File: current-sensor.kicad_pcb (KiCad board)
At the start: 2 copper layers, 78 x 39.3 mm, 36 parts, among them J1 ‎0197134001‎, J2 ‎0197134001‎, J3 0731000105, J4 Molex_SL_01x02_Male, J5 Molex_SL_01x02_Male, SW1 PN12SHNA03QE, SW2 OS103011MA7QP1, SW3 OS103011MA7QP1, U1 ACS730xLCTR-20AB, U2 AD8616xRM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

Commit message: revision 1 of current sensor
- fix gain/bandwidth switch pin numbering
- move faston connectors further apart
- switch from MSOP to SOIC package for op-amp
- add silk labels to switches and connectors
- reduce LED resistor to increase brightness
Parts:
- R8: value 3.3k -> 2.2k
- U2, U3: footprint Package_SO:MSOP-8_3x3mm_P0.65mm -> Package_SO:SOIC-8_3.9x4.9mm_P1.27mm
- moved R6 2.00 mm to (142.0, 98.0)
- moved J2 1.50 mm to (153.5, 73.0)
- moved C6 0.75 mm to (138.5, 96.5)
- moved C7 0.75 mm to (150.5, 89.2)
- moved R5 0.75 mm to (138.5, 93.2)
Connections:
- SW2 pad 1: Net-(R1-Pad2) -> Net-(R2-Pad2)
- SW2 pad 2: Net-(R2-Pad2) -> Net-(R1-Pad2)
- SW3 pad 1: Net-(R5-Pad1) -> Net-(C3-Pad2)
- SW3 pad 2: Net-(C3-Pad2) -> Net-(R5-Pad1)
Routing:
- net /virtual_gnd: track 58.2 -> 36.4 mm
- net Net-(R5-Pad1): track 15.9 -> 31.0 mm
- net Net-(R1-Pad2): track 19.7 -> 33.0 mm
- net Net-(R2-Pad2): track 3.21 -> 5.33 mm
- net Net-(C3-Pad2): track 3.21 -> 5.33 mm
- net +5V: track 98.6 -> 97.5 mm
- net Net-(C5-Pad1): track 7.78 -> 6.84 mm
- net Net-(R7-Pad2): track 6.20 -> 7.09 mm
- net /current-: track 11.5 -> 12.1 mm, vias 30 -> 29
- net Net-(R2-Pad1): track 14.5 -> 15.1 mm
- net (no net): vias 1 -> 2
- added copper zone on F.Cu, net /virtual_gnd
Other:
- board text added: "Current Sensor r1 G. Keeth github.com/gkeeth/current-sensor 2020-12-07"
- board text removed: "Current Sensor r1 G. Keeth github.com/gkeeth/current-sensor 2020-11-10"

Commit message: add zero-current offset trim
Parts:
- added C10: 100n, Capacitor_SMD:C_0603_1608Metric, F.Cu at (155.2, 86.4)
- added R10: 1M, Resistor_SMD:R_0603_1608Metric, F.Cu at (162.5, 86.2)
- added R9: 33k, Resistor_SMD:R_0603_1608Metric, F.Cu at (160.0, 85.5)
- added RV1: 100k, Potentiometer_SMD:Potentiometer_Vishay_TS53YL_Vertical, F.Cu at (170.5, 86.8)
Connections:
- U3 pad 5: Net-(C5-Pad1) -> Net-(C10-Pad1)
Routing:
- net Net-(R10-Pad2): track 0.00 -> 10.0 mm
- net Net-(C10-Pad1): track 0.00 -> 7.95 mm
- net +5V: track 97.5 -> 104.6 mm
- net Net-(C5-Pad1): track 6.84 -> 3.79 mm
- net GND: track 14.6 -> 17.2 mm, vias 9 -> 11
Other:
- board text added: "Current Sensor r2 G. Keeth github.com/gkeeth/current-sensor 2021-01-03"
- board text added: "Zero Current Offset Trim Procedure: 1. set 1x gain 2. apply zero current (open circuit at current terminals) 3. adjust trimmer until zero-current voltage (BNC output) and BNC ground are the same 4. increase gain to 10x/100x and fine-tune adjustment"
- board text removed: "Current Sensor r1 G. Keeth github.com/gkeeth/current-sensor 2020-12-07"

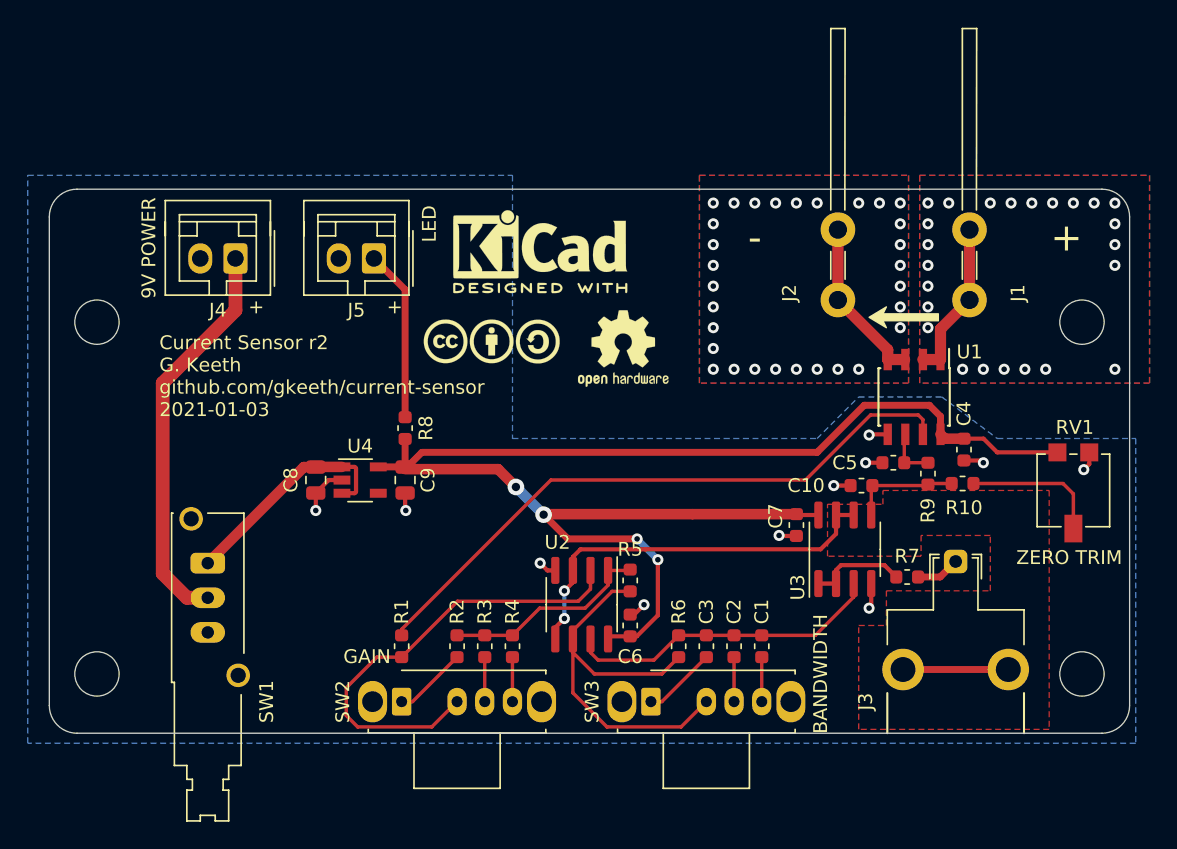
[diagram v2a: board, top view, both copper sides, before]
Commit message: Change offset trim circuit
completely ignore reference output from current sensor IC. Instead, use
trimpot to get 2.5V +/- 200mV reference voltage.
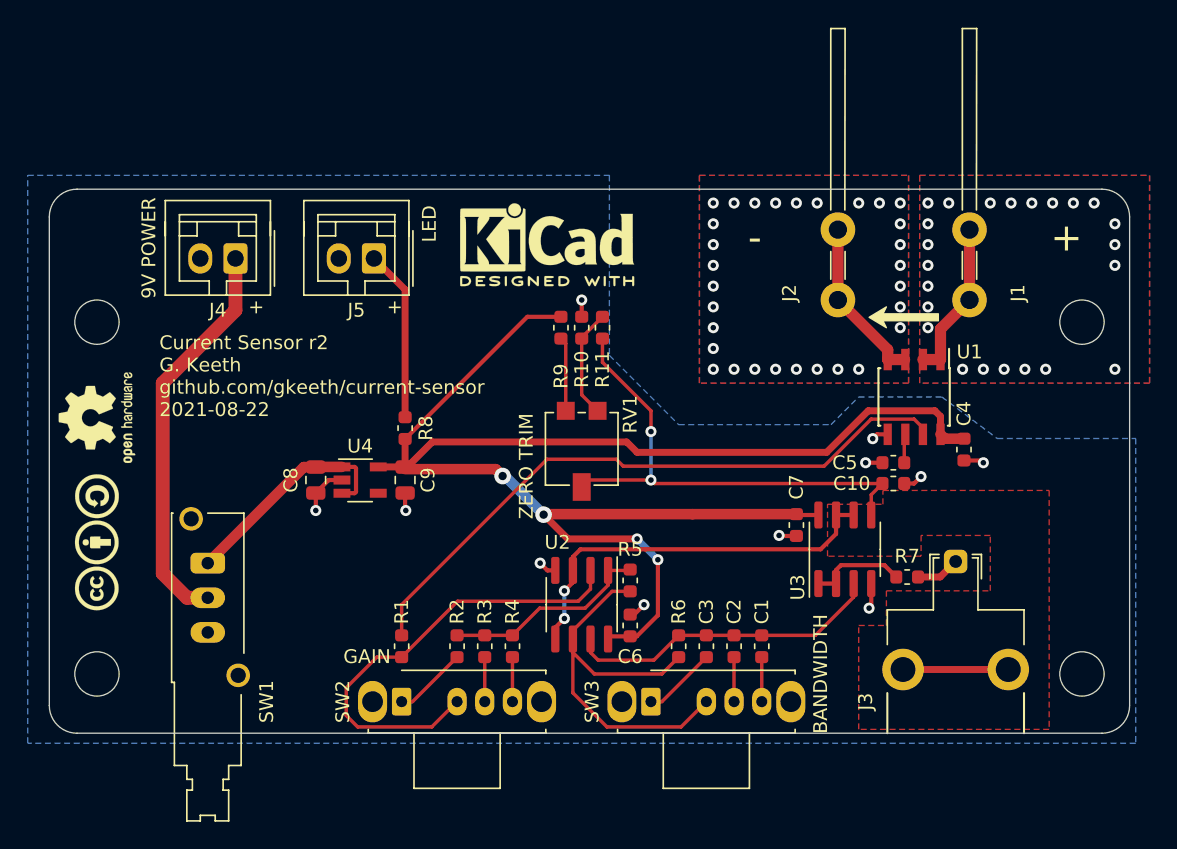
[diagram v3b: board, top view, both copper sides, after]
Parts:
- added R11: 1M, Resistor_SMD:R_0603_1608Metric, F.Cu at (136.5, 75.0)
- R10: value 1M -> 51k
- R9: value 33k -> 51k
- RV1: value 100k -> 10k
- moved LOGO3 38.3 mm to (100.0, 81.5), turned to 90 degrees
- moved RV1 35.6 mm to (135.0, 83.8)
- moved LOGO1 32.0 mm to (100.0, 90.5), turned to 90 degrees
- moved R10 29.7 mm to (135.0, 75.0), turned to 270 degrees
- moved R9 28.5 mm to (133.5, 75.0)
- moved C10 2.30 mm to (157.5, 86.2), turned to 0 degrees
- moved LOGO2 0.71 mm to (132.5, 69.0)
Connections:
- R10 pad 1: Net-(C10-Pad1) -> GND
- R9 pad 1: Net-(C10-Pad1) -> Net-(R9-Pad1)
- R9 pad 2: Net-(C5-Pad1) -> +5V
- RV1 pad 1: +5V -> Net-(R9-Pad1)
- RV1 pad 2: Net-(R10-Pad2) -> Net-(C10-Pad1)
- RV1 pad 3: GND -> Net-(R10-Pad2)
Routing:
- net Net-(C10-Pad1): track 7.95 -> 36.3 mm, vias 0 -> 2
- net +5V: track 104.6 -> 112.7 mm
- net Net-(R9-Pad1): track 0.00 -> 5.36 mm
- net Net-(R10-Pad2): track 10.0 -> 7.89 mm
- net Net-(C5-Pad1): track 3.79 -> 2.08 mm
- net Net-(R1-Pad1): track 45.7 -> 46.5 mm
- net /current-: vias 29 -> 30
- net (no net): vias 2 -> 0
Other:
- board text added: "Current Sensor r2 G. Keeth github.com/gkeeth/current-sensor 2021-08-22"
- board text removed: "Current Sensor r2 G. Keeth github.com/gkeeth/current-sensor 2021-01-03"
